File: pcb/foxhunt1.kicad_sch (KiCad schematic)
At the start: 0 parts

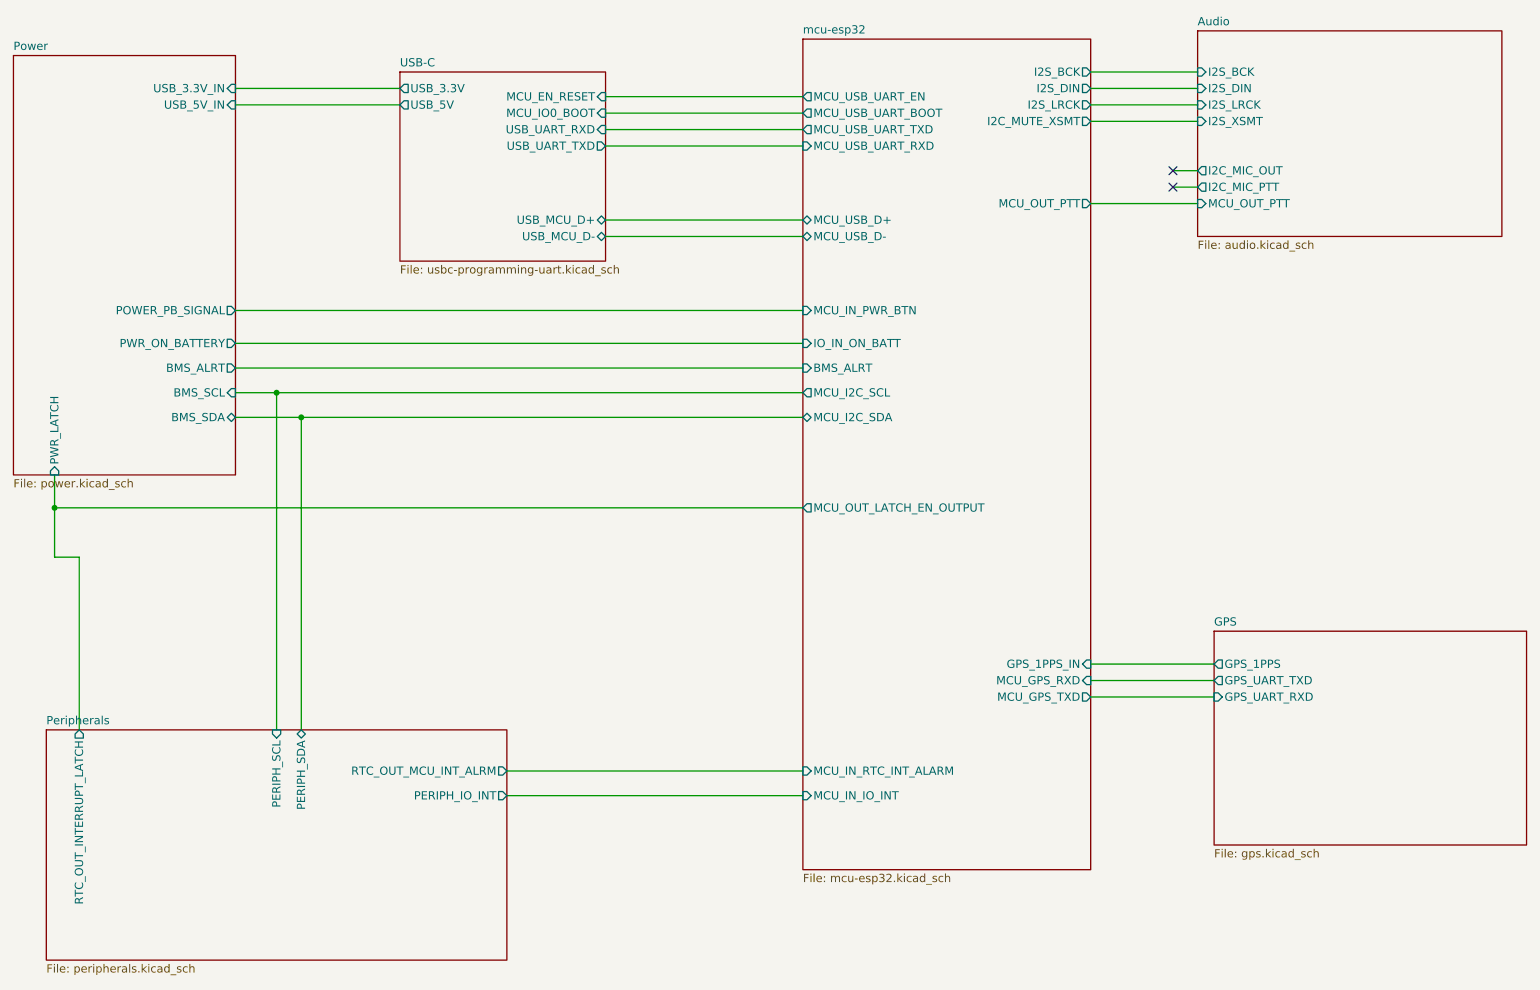
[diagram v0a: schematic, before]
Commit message: Add SA818S-V sheet, update GPS antenna connector, MCU GPIO reassignments
- New SA818S-V sheet (U19): UART/PTT/MIC_IN wired; VBAT, ANT, PD, H/L
  still open (see sa818_pinout.md).
- gps.kicad_sch: J10 swapped to Amphenol 132289 edge-launch SMD SMA
  (same part planned for the SA818 antenna connector).
- mcu-esp32.kicad_sch: SA818 UART on IO6/IO7, PTT on IO16 (direct FET
  drive via Q10, not the originally-planned AND-gate scheme).
- peripherals.kicad_sch: in-progress PCA9555 channel changes.

Co-Authored-By: Claude Sonnet 5 <noreply@anthropic.com>
Claude-Session: https://claude.ai/code/session_01LhLkuH6sQ5GbUZ61bG7p2h
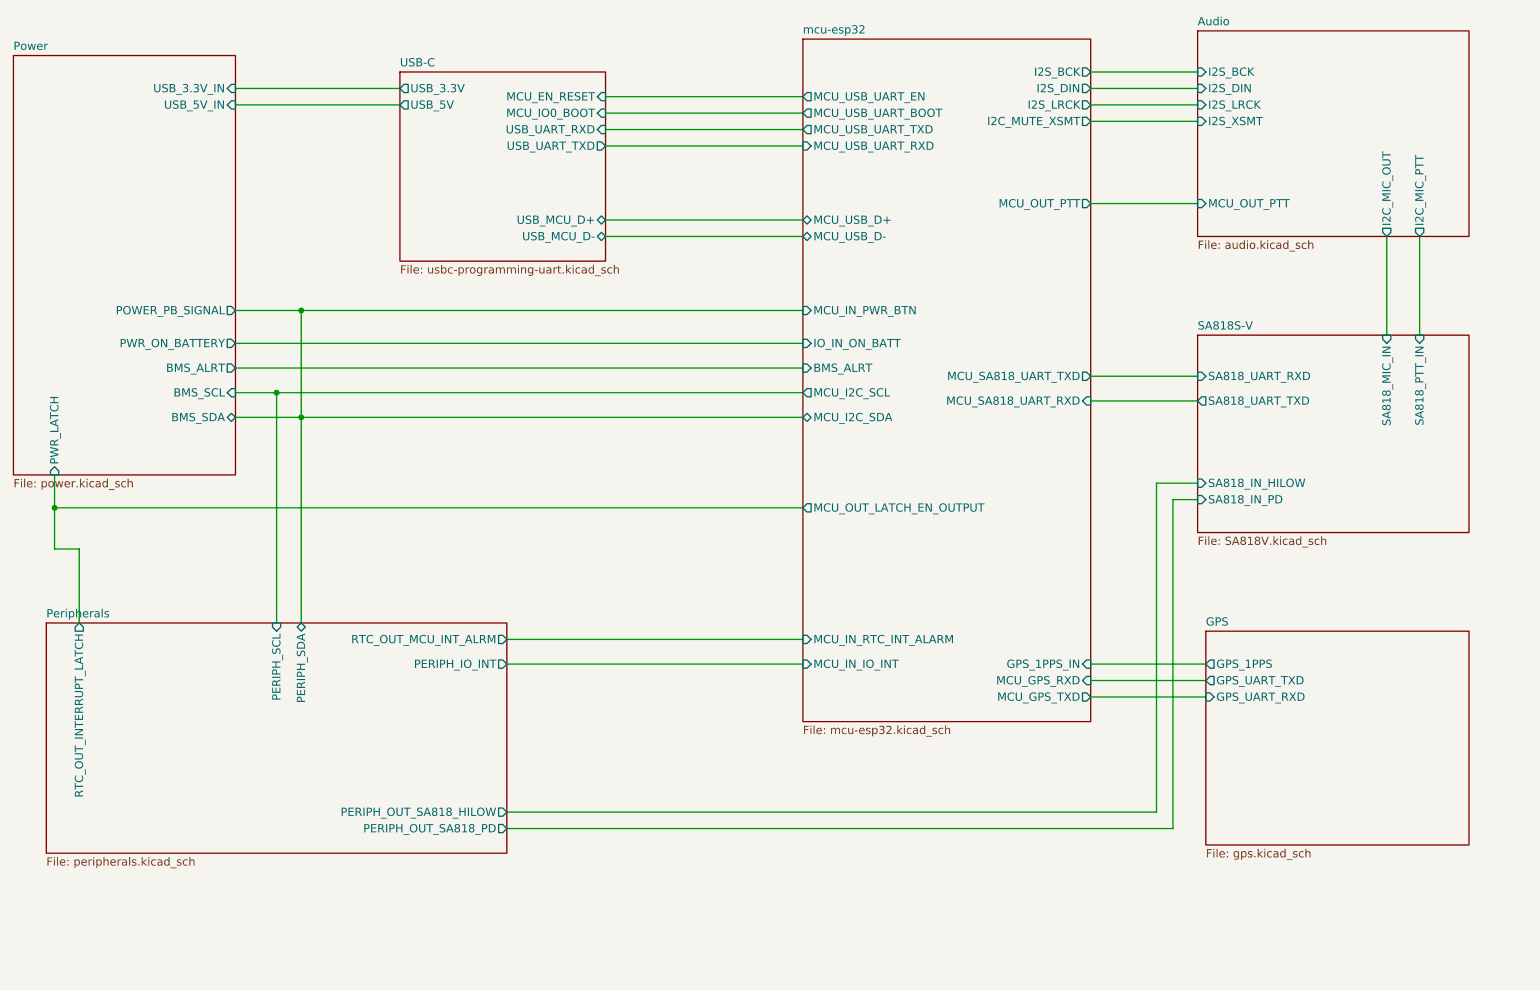
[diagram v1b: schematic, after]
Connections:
- no-connect marks 2 -> 0
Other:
- added sheet SA818S-V (SA818V.kicad_sch)
- sheet Peripherals ports: added PERIPH_OUT_SA818_HILOW, PERIPH_OUT_SA818_PD; removed none
- sheet mcu-esp32 ports: added MCU_SA818_UART_RXD, MCU_SA818_UART_TXD; removed none

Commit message: Wire SA818 PD/H-L and PTT opto, GPS power gating with bench bypass, RF detector groundwork
- SA818S-V: wire PD/H-L to PCA9555 expander outputs; swap PTT-keying FET
  for PC817 optocoupler isolation on the shared SA818S/external-HT PTT line
- GPS: add Q10 (AO3407A) high-side P-FET gating VCC+VCC_IO together for
  genuine hardware backup mode, driven via Q13 level-shifter from a new
  PCA9555 output (PERIPH_OUT_GPS_PWRON); add JP28 as a source-to-drain
  bench bypass across Q10 for unconditional power during bring-up; wire
  EXTINT to another PCA9555 output (PERIPH_OUT_GPS_EXTINT, pulled low by
  R57) to experiment with UART software-standby + external wake
- peripherals: reassign PCA9555 channels for the above plus SA818 PD/H-L
- audio/mcu-esp32: forward-power detector tap wiring groundwork
- docs: add vhf_matching_detector.md (matching network + RF detector BOM
  and layout), index it in _docs/README.md

Co-Authored-By: Claude Sonnet 5 <noreply@anthropic.com>
Claude-Session: https://claude.ai/code/session_01LhLkuH6sQ5GbUZ61bG7p2h
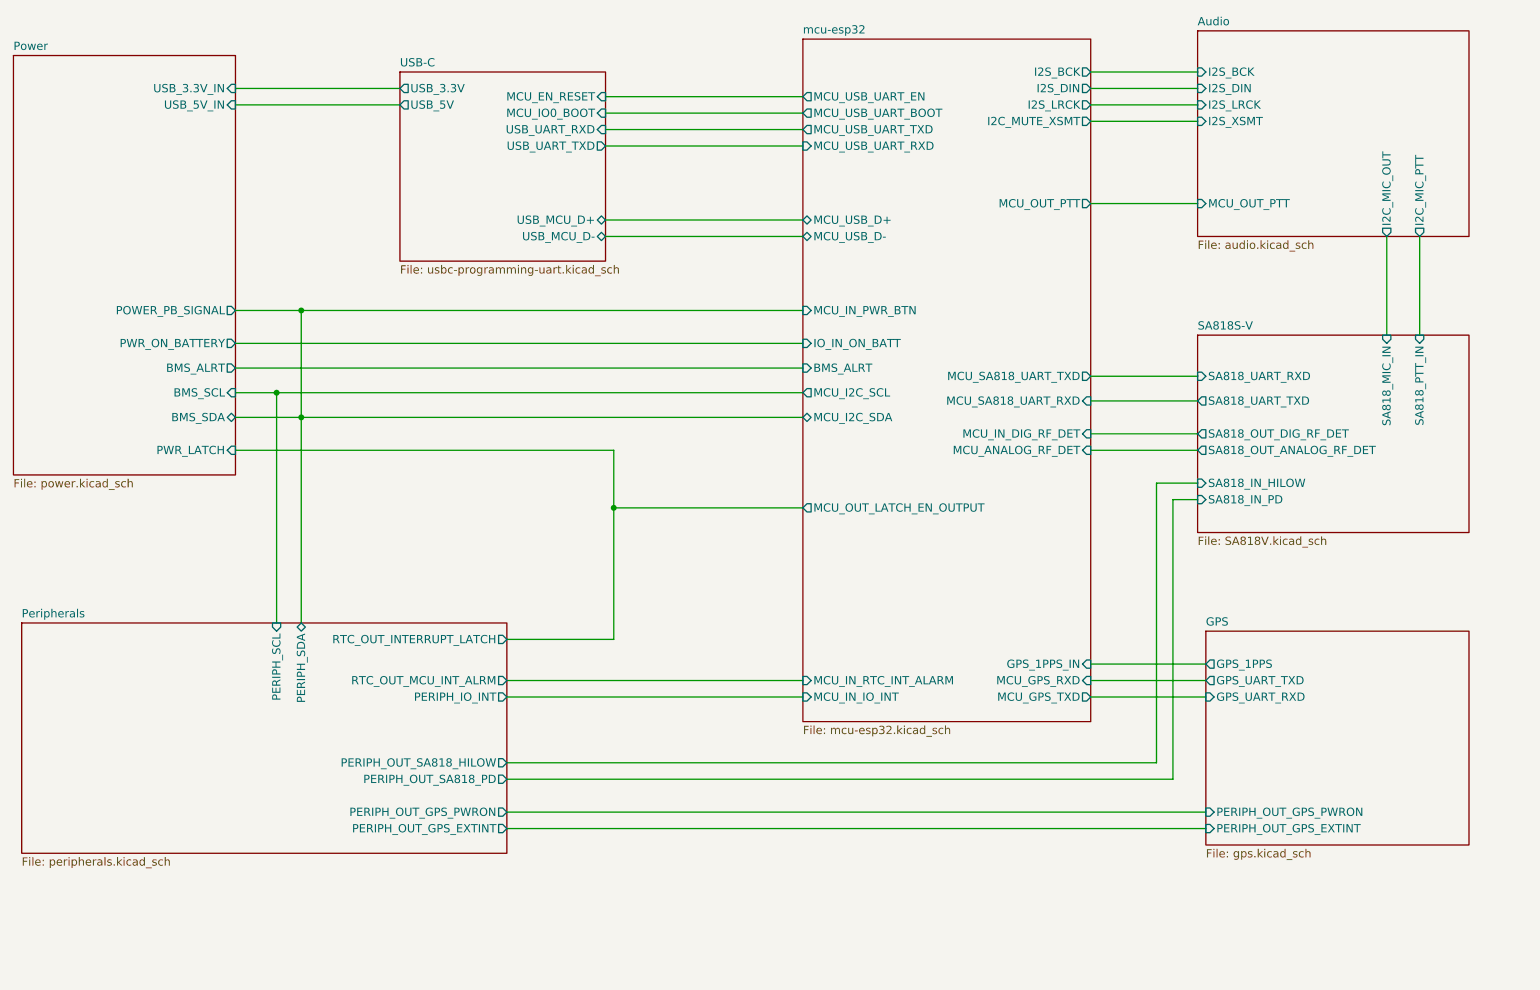
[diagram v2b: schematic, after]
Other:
- sheet GPS ports: added PERIPH_OUT_GPS_EXTINT, PERIPH_OUT_GPS_PWRON; removed none
- sheet Peripherals ports: added PERIPH_OUT_GPS_EXTINT, PERIPH_OUT_GPS_PWRON; removed none
- sheet SA818S-V ports: added SA818_OUT_ANALOG_RF_DET, SA818_OUT_DIG_RF_DET; removed none
- sheet mcu-esp32 ports: added MCU_ANALOG_RF_DET, MCU_IN_DIG_RF_DET; removed none
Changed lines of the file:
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@@
+	)
+	(junction
+		(at 137.16 105.41)
+		(diameter 0)
+		(color 0 0 0 0)
 	)
 	(junction
@@
 		(color 0 0 0 0)
 	)
-	(junction
-		(at 50.8 105.41)
-		(diameter 0)
-		(color 0 0 0 0)
-	)
-	(wire
-		(pts
-			(xy 54.61 111.76) (xy 54.61 123.19)
-		)
-		(stroke
-			(width 0)
-			(type default)
-		)
-	)
 	(wire
 		(pts
@@
 	(wire
 		(pts
-			(xy 50.8 111.76) (xy 54.61 111.76)
-		)
-		(stroke
-			(width 0)
-			(type default)
-		)
-	)
-	(wire
-		(pts
 			(xy 210.82 40.64) (xy 227.33 40.64)
 		)
@@
 	(wire
 		(pts
+			(xy 210.82 93.98) (xy 227.33 93.98)
+		)
+		(stroke
+			(width 0)
+			(type default)
+		)
+	)
+	(wire
+		(pts
+			(xy 120.65 152.4) (xy 228.6 152.4)
+		)
+		(stroke
+			(width 0)
+			(type default)
+		)
+	)
+	(wire
+		(pts
 			(xy 78.74 91.44) (xy 88.9 91.44)
 		)
@@
 	(wire
 		(pts
-			(xy 220.98 101.6) (xy 220.98 152.4)
-		)
-		(stroke
-			(width 0)
-			(type default)
-		)
-	)
-	(wire
-		(pts
-			(xy 120.65 129.54) (xy 166.37 129.54)
+			(xy 220.98 101.6) (xy 220.98 144.78)
 		)
 		(stroke
@@
 	(wire
 		(pts
+			(xy 210.82 96.52) (xy 227.33 96.52)
+		)
+		(stroke
+			(width 0)
+			(type default)
+		)
+	)
+	(wire
+		(pts
 			(xy 210.82 129.54) (xy 228.6 129.54)
 		)
@@
 	(wire
 		(pts
+			(xy 137.16 96.52) (xy 137.16 105.41)
+		)
+		(stroke
+			(width 0)
+			(type default)
+		)
+	)
+	(wire
+		(pts
 			(xy 227.33 101.6) (xy 220.98 101.6)
 		)
@@
 	(wire
 		(pts
+			(xy 78.74 96.52) (xy 137.16 96.52)
+		)
+		(stroke
+			(width 0)
+			(type default)
+		)
+	)
+	(wire
+		(pts
+			(xy 120.65 134.62) (xy 166.37 134.62)
+		)
+		(stroke
+			(width 0)
+			(type default)
+		)
+	)
+	(wire
+		(pts
 			(xy 256.54 63.5) (xy 256.54 78.74)
 		)
@@
 	(wire
 		(pts
-			(xy 220.98 152.4) (xy 120.65 152.4)
+			(xy 137.16 105.41) (xy 166.37 105.41)
+		)
+		(stroke
+			(width 0)
+			(type default)
+		)
+	)
+	(wire
+		(pts
+			(xy 220.98 144.78) (xy 120.65 144.78)
+		)
+		(stroke
+			(width 0)
+			(type default)
+		)
+	)
+	(wire
+		(pts
+			(xy 137.16 125.73) (xy 137.16 105.41)
+		)
+		(stroke
+			(width 0)
+			(type default)
+		)
+	)
+	(wire
+		(pts
+			(xy 120.65 154.94) (xy 228.6 154.94)
 		)
 		(stroke
@@
 	(wire
 		(pts
-			(xy 50.8 111.76) (xy 50.8 105.41)
-		)
-		(stroke
-			(width 0)
-			(type default)
-		)
-	)
-	(wire
-		(pts
 			(xy 210.82 58.42) (xy 227.33 58.42)
 		)
@@
 	(wire
 		(pts
+			(xy 120.65 125.73) (xy 137.16 125.73)
+		)
+		(stroke
+			(width 0)
+			(type default)
+		)
+	)
+	(wire
+		(pts
 			(xy 210.82 38.1) (xy 227.33 38.1)
 		)
@@
 	(wire
 		(pts
-			(xy 50.8 105.41) (xy 166.37 105.41)
-		)
-		(stroke
-			(width 0)
-			(type default)
-		)
-	)
-	(wire
-		(pts
-			(xy 120.65 125.73) (xy 166.37 125.73)
+			(xy 120.65 132.08) (xy 166.37 132.08)
 		)
 		(stroke
@@
 	(wire
 		(pts
-			(xy 223.52 154.94) (xy 223.52 104.14)
+			(xy 223.52 147.32) (xy 223.52 104.14)
 		)
 		(stroke
@@
 	(wire
 		(pts
-			(xy 50.8 105.41) (xy 50.8 100.33)
-		)
-		(stroke
-			(width 0)
-			(type default)
-		)
-	)
-	(wire
-		(pts
 			(xy 135.89 44.45) (xy 166.37 44.45)
 		)
@@
 	(wire
 		(pts
-			(xy 120.65 154.94) (xy 223.52 154.94)
+			(xy 120.65 147.32) (xy 223.52 147.32)
 		)
 		(stroke
@@
 			)
 		)
+		(pin "PERIPH_OUT_GPS_PWRON" input
+			(at 228.6 152.4 180)
+			(effects
+				(font
+					(size 1.27 1.27)
+				)
+				(justify left)
+			)
+		)
+		(pin "PERIPH_OUT_GPS_EXTINT" input
+			(at 228.6 154.94 180)
+			(effects
+				(font
+					(size 1.27 1.27)
+				)
+				(justify left)
+			)
+		)
 		(instances
 			(project "foxhunt1"
@@
 			)
 		)
+		(pin "SA818_OUT_ANALOG_RF_DET" output
+			(at 227.33 96.52 180)
+			(effects
+				(font
+					(size 1.27 1.27)
+				)
+				(justify left)
+			)
+		)
+		(pin "SA818_OUT_DIG_RF_DET" output
+			(at 227.33 93.98 180)
+			(effects
+				(font
+					(size 1.27 1.27)
+				)
+				(justify left)
+			)
+		)
 		(instances
 			(project "foxhunt1"
@@
 		)
 		(pin "PWR_LATCH" input
-			(at 50.8 100.33 270)
-			(effects
-				(font
-					(size 1.27 1.27)
-				)
-				(justify left)
+			(at 78.74 96.52 0)
+			(effects
+				(font
+					(size 1.27 1.27)
+				)
+				(justify right)
 			)
 		)
@@
 		)
 		(pin "MCU_IN_RTC_INT_ALARM" input
-			(at 166.37 125.73 180)
+			(at 166.37 132.08 180)
 			(effects
 				(font
@@
 		)
 		(pin "MCU_IN_IO_INT" input
-			(at 166.37 129.54 180)
+			(at 166.37 134.62 180)
 			(effects
 				(font
@@
 		(pin "MCU_SA818_UART_TXD" output
 			(at 210.82 85.09 0)
+			(effects
+				(font
+					(size 1.27 1.27)
+				)
+				(justify right)
+			)
+		)
+		(pin "MCU_ANALOG_RF_DET" input
+			(at 210.82 96.52 0)
+			(effects
+				(font
+					(size 1.27 1.27)
+				)
+				(justify right)
+			)
+		)
+		(pin "MCU_IN_DIG_RF_DET" input
+			(at 210.82 93.98 0)
 			(effects
 				(font
@@
 	)
 	(sheet
-		(at 49.53 123.19)
-		(size 71.12 35.56)
+		(at 45.72 123.19)
+		(size 74.93 35.56)
 		(exclude_from_sim no)
 		(in_bom yes)
@@
 		)
 		(property "Sheetname" "Peripherals"
-			(at 49.53 122.4784 0)
+			(at 45.72 122.4784 0)
 			(show_name no)
 			(do_not_autoplace no)
@@
 		)
 		(property "Sheetfile" "peripherals.kicad_sch"
-			(at 49.53 159.3346 0)
+			(at 45.72 159.3346 0)
 			(show_name no)
 			(do_not_autoplace no)
@@
 		)
 		(pin "RTC_OUT_INTERRUPT_LATCH" output
-			(at 54.61 123.19 90)
+			(at 120.65 125.73 0)
 			(effects
 				(font
@@
 		)
 		(pin "RTC_OUT_MCU_INT_ALRM" output
-			(at 120.65 125.73 0)
+			(at 120.65 132.08 0)
 			(effects
 				(font
@@
 		)
 		(pin "PERIPH_IO_INT" output
-			(at 120.65 129.54 0)
+			(at 120.65 134.62 0)
 			(effects
 				(font
@@
 		)
 		(pin "PERIPH_OUT_SA818_HILOW" output
+			(at 120.65 144.78 0)
+			(effects
+				(font
+					(size 1.27 1.27)
+				)
+				(justify right)
+			)
+		)
+		(pin "PERIPH_OUT_SA818_PD" output
+			(at 120.65 147.32 0)
+			(effects
+				(font
+					(size 1.27 1.27)
+				)
+				(justify right)
+			)
+		)
+		(pin "PERIPH_OUT_GPS_PWRON" output
 			(at 120.65 152.4 0)
 			(effects
@@
 			)
 		)
-		(pin "PERIPH_OUT_SA818_PD" output
+		(pin "PERIPH_OUT_GPS_EXTINT" output
 			(at 120.65 154.94 0)
 			(effects

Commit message: Move audio jack (J6) into SA818V sheet, rename nets/jumpers for clarity
Relocates the switched TRS jack from audio.kicad_sch into SA818V.kicad_sch
and updates the root sheet's pin interface to match (SA818_IN_MIC,
SA818_IN_PTT, new SA818_IN_PTT_HB), fixing an I2C_MIC_OUT/I2S_MIC_OUT
naming typo along the way. Ring/ring-switch/sleeve are wired; tip and
tip-switch (mic audio leg) are still open, per audio_ptt_path.md.

Also: renames GPS hierarchical labels and several power/regulation/
peripheral jumper values from generic (Jumper_2_Open, SolderJumper_2_Open)
to descriptive names, wires MCU_OUT_PTT_HB, and removes now-unused test
points/jumpers from the battery input sheets. Adds 74hc123_pinout.md
planning doc for the TX-safety timeout / force-off failsafe part.

Co-Authored-By: Claude Sonnet 5 <noreply@anthropic.com>
Claude-Session: https://claude.ai/code/session_01P3G1ionr2QCR8SZtKRreL3
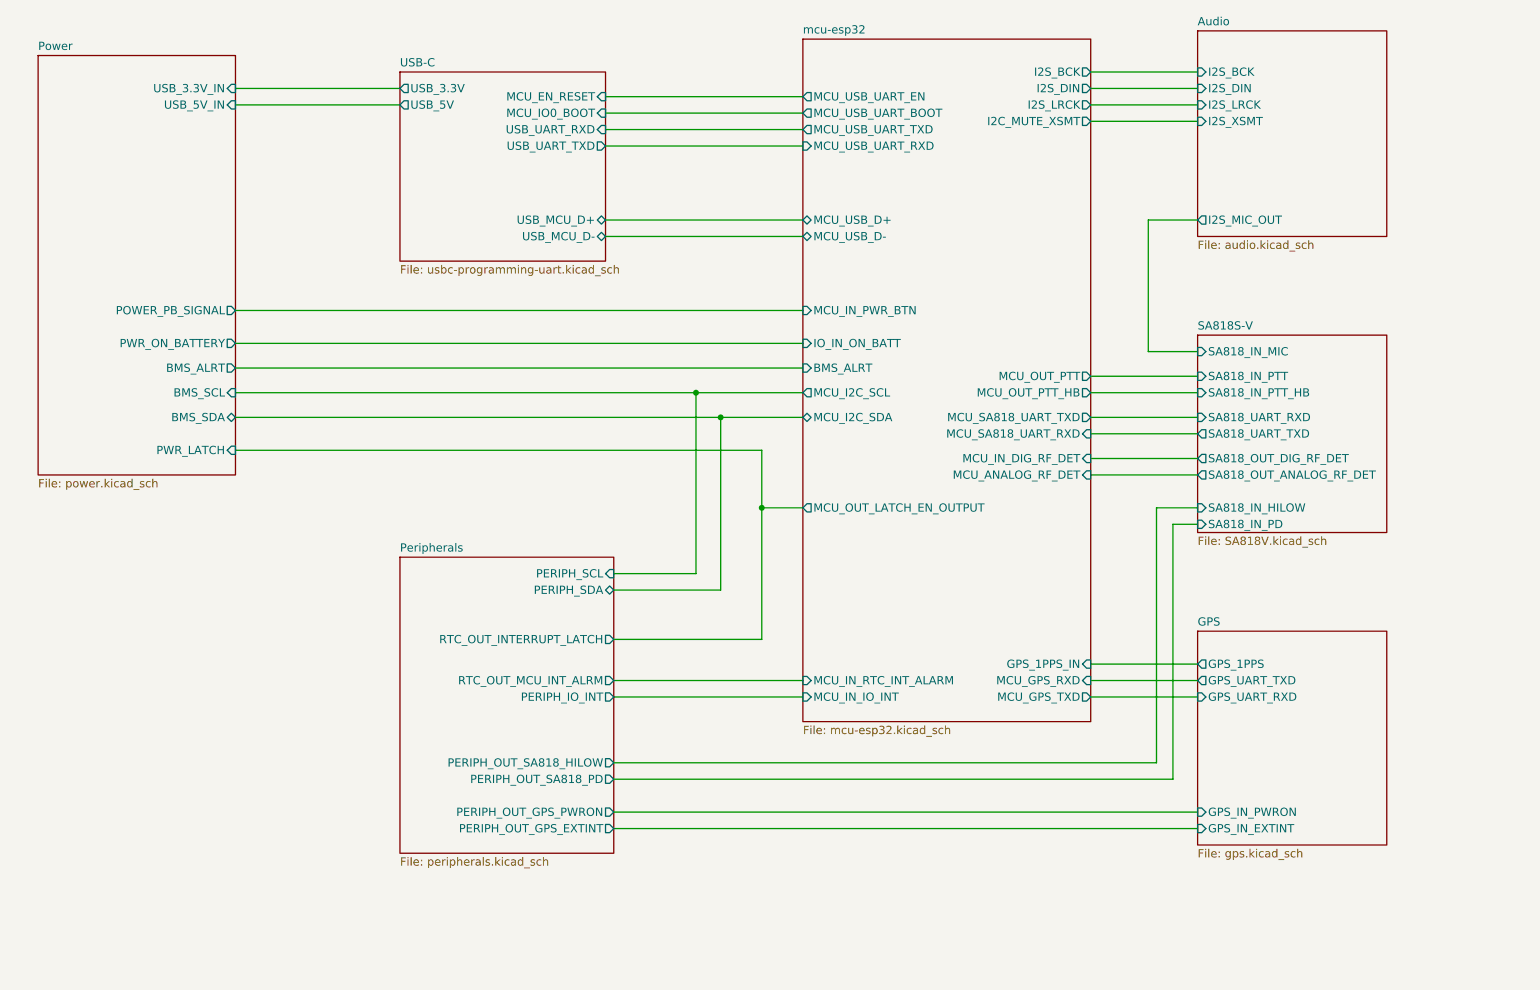
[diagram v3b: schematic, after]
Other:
- sheet Audio ports: added I2S_MIC_OUT; removed I2C_MIC_OUT, I2C_MIC_PTT, MCU_OUT_PTT
- sheet GPS ports: added GPS_IN_EXTINT, GPS_IN_PWRON; removed PERIPH_OUT_GPS_EXTINT, PERIPH_OUT_GPS_PWRON
- sheet SA818S-V ports: added SA818_IN_MIC, SA818_IN_PTT, SA818_IN_PTT_HB; removed SA818_MIC_IN, SA818_PTT_IN
- sheet mcu-esp32 ports: added MCU_OUT_PTT_HB; removed none
